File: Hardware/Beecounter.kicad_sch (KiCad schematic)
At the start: 142 parts, among them J1 Conn_01x03, J10 Conn_01x03, J11 Conn_01x03, J12 Conn_01x03, J13 Conn_01x03, J14 Conn_01x03, J15 Conn_02x20_Odd_Even, J2 Conn_01x03, J3 Conn_01x03, J4 Conn_01x03, J5 Conn_01x03, J6 Conn_01x03, J7 Conn_01x03, J8 Conn_01x03, J9 Conn_01x03, U1 LM393, U10 LM393, U11 H2010, U12 LM393, U13 H2010, U14 LM393, U15 H2010, U16 LM393, U17 H2010, U18 LM393, U19 H2010, U2 H2010, U20 LM393, U21 H2010, U22 LM393, U23 H2010, U24 LM393, U25 H2010, U26 LM393, U27 H2010, U28 LM393, U3 H2010, U4 LM393, U5 H2010, U6 LM393, U7 H2010, U8 LM393, U9 H2010

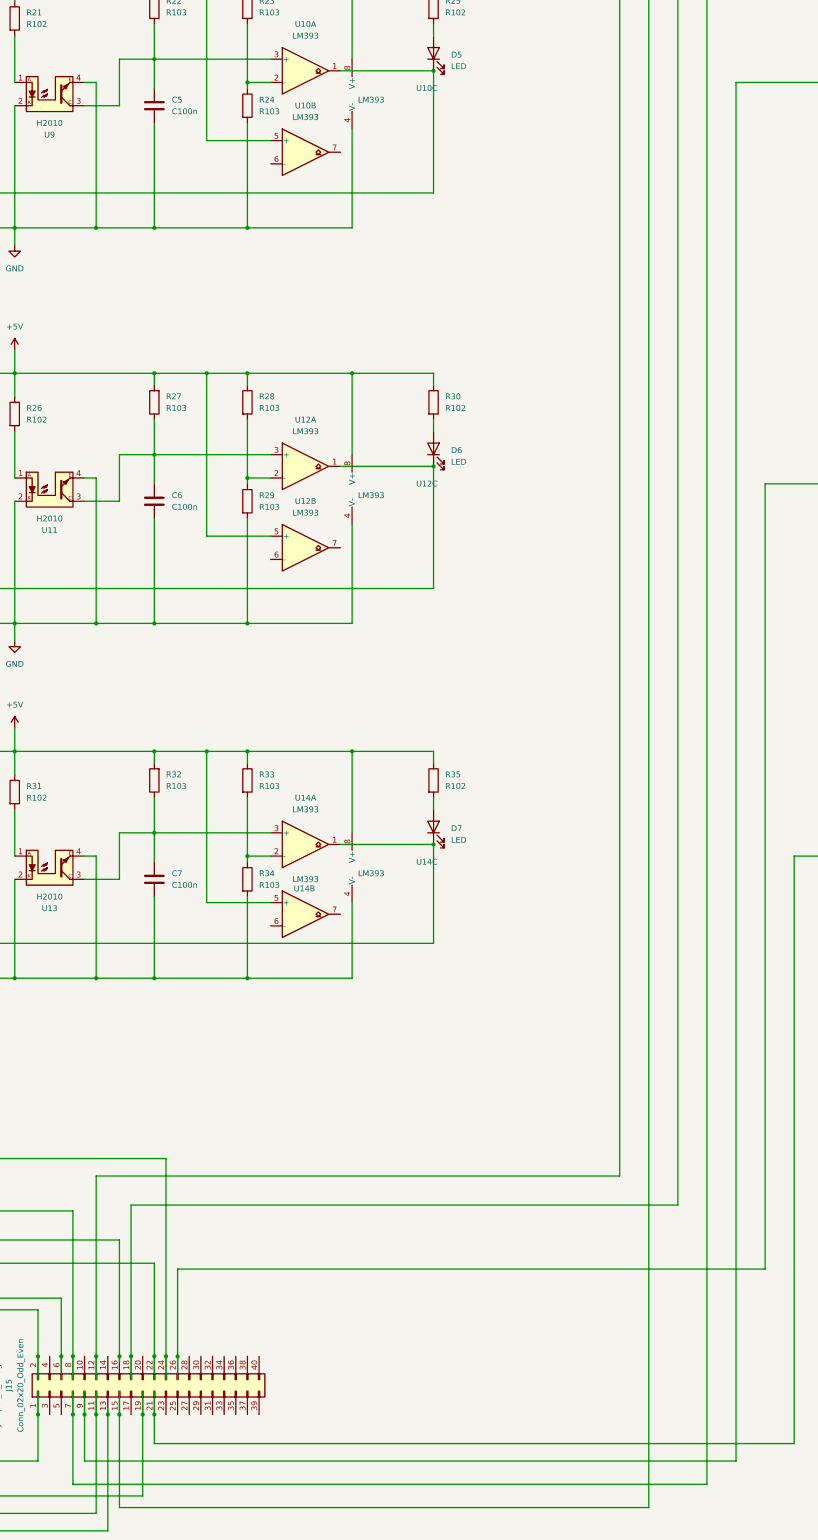
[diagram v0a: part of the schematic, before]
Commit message: Fix issue with entrance 5. Connected light barrier to pin 10 (GPIO16) instead of 9 (GND)
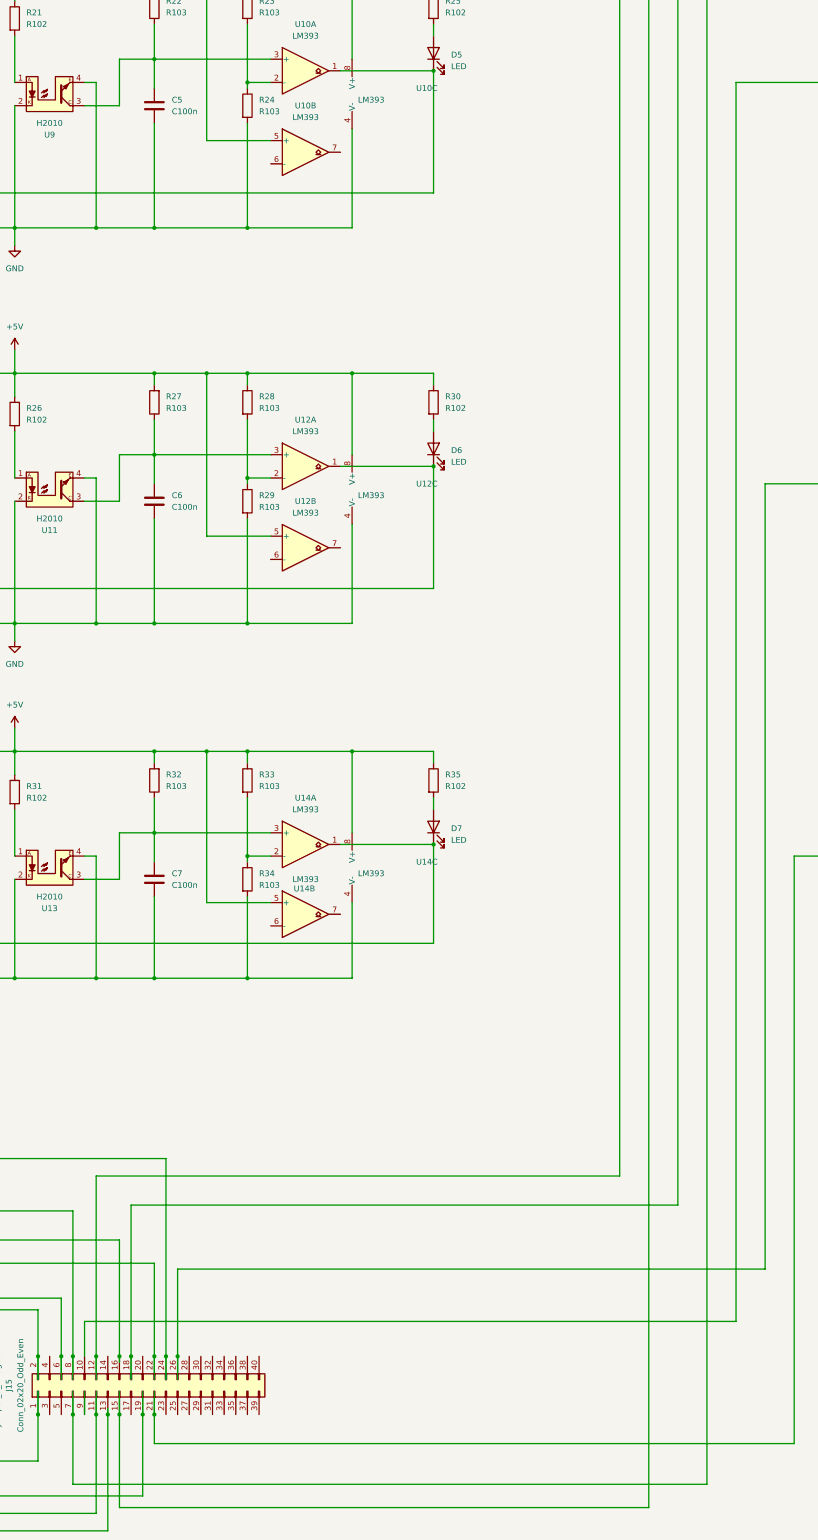
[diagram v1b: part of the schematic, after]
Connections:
- net at D12.1 (K), J12.2 (Pin_2), U24.1: now also J15.10 (Pin_10); no longer J15.9 (Pin_9)
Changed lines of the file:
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@@
 	)
 	(junction
-		(at 171.45 676.91)
-		(diameter 0)
-		(color 0 0 0 0)
-	)
-	(junction
 		(at 179.07 664.21)
 		(diameter 0)
@@
 	(wire
 		(pts
-			(xy 313.69 687.07) (xy 171.45 687.07)
+			(xy 313.69 656.59) (xy 171.45 656.59)
 		)
 		(stroke
@@
 	(wire
 		(pts
-			(xy 171.45 676.91) (xy 171.45 687.07)
-		)
-		(stroke
-			(width 0)
-			(type default)
-		)
-	)
-	(wire
-		(pts
 			(xy 80.01 474.98) (xy 133.35 474.98)
 		)
@@
 	(wire
 		(pts
-			(xy 313.69 386.08) (xy 313.69 687.07)
+			(xy 313.69 386.08) (xy 313.69 656.59)
 		)
 		(stroke
@@
 		)
 		(stroke
+			(width 0)
+			(type default)
+		)
+	)
+	(wire
+		(pts
+			(xy 171.45 656.59) (xy 171.45 664.21)
+		)
+		(stroke

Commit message: Set power supply for light barriers to 3.3V
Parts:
- removed JP1: Jumper_3_Bridged12, Jumper:SolderJumper-3_P1.3mm_Open_RoundedPad1.0x1.5mm, symbol Jumper:Jumper_3_Bridged12
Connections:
- net +5V is gone; now on net +3.3V: J1.1 (Pin_1), J10.1 (Pin_1), J11.1 (Pin_1), J12.1 (Pin_1), J13.1 (Pin_1), J14.1 (Pin_1), J2.1 (Pin_1), J3.1 (Pin_1), J4.1 (Pin_1), J5.1 (Pin_1), J6.1 (Pin_1), J7.1 (Pin_1), J8.1 (Pin_1), J9.1 (Pin_1), R1.1, R10.1, R11.1, R12.2, R13.1, R15.1, R16.1, R17.2, R18.1, R2.1, R20.1, R21.1, R22.2, R23.1, R25.1, R26.1, R27.2, R28.1, R30.1, R31.1, R32.2, R33.1, R35.1, R36.1, R37.2, R38.1, R4.2, R40.1, R41.1, R42.2, R43.1, R45.1, R46.1, R47.2, R48.1, R5.1, R50.1, R51.1, R52.2, R53.1, R55.1, R56.1, R57.2, R58.1, R6.1, R60.1, R61.1, R62.2, R63.1, R65.1, R66.1, R67.2, R68.1, R7.2, R70.1, R8.1, U1.5 (+), U1.8 (V+), U10.5 (+), U10.8 (V+), U12.5 (+), U12.8 (V+), U14.5 (+), U14.8 (V+), U16.5 (+), U16.8 (V+), U18.5 (+), U18.8 (V+), U20.5 (+), U20.8 (V+), U22.5 (+), U22.8 (V+), U24.5 (+), U24.8 (V+), U26.5 (+), U26.8 (V+), U28.5 (+), U28.8 (V+), U4.5 (+), U4.8 (V+), U6.5 (+), U6.8 (V+), U8.5 (+), U8.8 (V+)
- net +3.3V: now reaches J15.1 (Pin_1)
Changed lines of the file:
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@@
 	)
 	(junction
-		(at 161.29 664.21)
-		(diameter 0)
-		(color 0 0 0 0)
-	)
-	(junction
 		(at 198.12 36.83)
 		(diameter 0)
@@
 	)
 	(junction
-		(at 142.24 670.56)
-		(diameter 0)
-		(color 0 0 0 0)
-	)
-	(junction
 		(at 459.74 59.69)
 		(diameter 0)
@@
 	)
 	(junction
-		(at 146.05 676.91)
-		(diameter 0)
-		(color 0 0 0 0)
-	)
-	(junction
 		(at 436.88 250.19)
 		(diameter 0)
@@
 	)
 	(junction
-		(at 146.05 664.21)
-		(diameter 0)
-		(color 0 0 0 0)
-	)
-	(junction
 		(at 454.66 415.29)
 		(diameter 0)
@@
 	(wire
 		(pts
-			(xy 161.29 687.07) (xy 146.05 687.07)
-		)
-		(stroke
-			(width 0)
-			(type default)
-		)
-	)
-	(wire
-		(pts
 			(xy 156.21 477.52) (xy 156.21 504.19)
 		)
@@
 	(wire
 		(pts
-			(xy 146.05 664.21) (xy 146.05 665.48)
-		)
-		(stroke
-			(width 0)
-			(type default)
-		)
-	)
-	(wire
-		(pts
 			(xy 453.39 529.59) (xy 453.39 532.13)
 		)
@@
 	(wire
 		(pts
-			(xy 142.24 670.56) (xy 144.78 670.56)
-		)
-		(stroke
-			(width 0)
-			(type default)
-		)
-	)
-	(wire
-		(pts
 			(xy 184.15 694.69) (xy 184.15 676.91)
 		)
@@
 	(wire
 		(pts
-			(xy 146.05 675.64) (xy 146.05 676.91)
-		)
-		(stroke
-			(width 0)
-			(type default)
-		)
-	)
-	(wire
-		(pts
 			(xy 477.52 481.33) (xy 477.52 502.92)
 		)
@@
 	(wire
 		(pts
-			(xy 161.29 654.05) (xy 146.05 654.05)
-		)
-		(stroke
-			(width 0)
-			(type default)
-		)
-	)
-	(wire
-		(pts
 			(xy 478.79 278.13) (xy 496.57 278.13)
 		)
@@
 	(wire
 		(pts
-			(xy 146.05 687.07) (xy 146.05 676.91)
-		)
-		(stroke
-			(width 0)
-			(type default)
-		)
-	)
-	(wire
-		(pts
 			(xy 434.34 466.09) (xy 434.34 472.44)
 		)
@@
 	(wire
 		(pts
-			(xy 146.05 664.21) (xy 146.05 654.05)
-		)
-		(stroke
-			(width 0)
-			(type default)
-		)
-	)
-	(wire
-		(pts
 			(xy 133.35 472.44) (xy 140.97 472.44)
 		)
@@
 	(wire
 		(pts
-			(xy 118.11 670.56) (xy 142.24 670.56)
+			(xy 118.11 687.07) (xy 161.29 687.07)
 		)
 		(stroke
@@
 	(wire
 		(pts
-			(xy 161.29 664.21) (xy 161.29 654.05)
-		)
-		(stroke
-			(width 0)
-			(type default)
-		)
-	)
-	(wire
-		(pts
 			(xy 403.86 415.29) (xy 421.64 415.29)
 		)
@@
 	(wire
 		(pts
-			(xy 118.11 670.56) (xy 118.11 554.99)
+			(xy 118.11 687.07) (xy 118.11 554.99)
 		)
 		(stroke
@@
 			)
 		)
-		(property "Value" "+5V"
+		(property "Value" "+3.3V"
 			(at 156.21 353.06 0)
 			(effects
@@
 			)
 		)
-		(property "Value" "+5V"
+		(property "Value" "+3.3V"
 			(at 403.86 350.52 0)
 			(effects
@@
 			)
 		)
-		(property "Value" "+5V"
+		(property "Value" "+3.3V"
 			(at 407.67 102.87 0)
 			(effects
@@
 			)
 		)
-		(property "Value" "+5V"
+		(property "Value" "+3.3V"
 			(at 403.86 438.15 0)
 			(effects
@@
 			)
 		)
-		(property "Value" "+5V"
+		(property "Value" "+3.3V"
 			(at 156.21 270.51 0)
 			(effects
@@
 	)
 	(symbol
-		(lib_id "Jumper:Jumper_3_Bridged12")
-		(at 146.05 670.56 270)
-		(unit 1)
-		(exclude_from_sim yes)
-		(in_bom no)
-		(on_board yes)
-		(dnp no)
-		(fields_autoplaced yes)
-		(property "Reference" "JP1"
-			(at 149.86 670.56 0)
-			(effects
-				(font
-					(size 1.27 1.27)
-				)
-			)
-		)
-		(property "Value" "Jumper_3_Bridged12"
-			(at 152.4 670.56 0)
-			(effects
-				(font
-					(size 1.27 1.27)
-				)
-			)
-		)
-		(property "Footprint" "Jumper:SolderJumper-3_P1.3mm_Open_RoundedPad1.0x1.5mm"
-			(at 146.05 670.56 0)
-			(effects
-				(font
-					(size 1.27 1.27)
-				)
-				(hide yes)
-			)
-		)
-		(property "Datasheet" "~"
-			(at 146.05 670.56 0)
-			(effects
-				(font
-					(size 1.27 1.27)
-				)
-				(hide yes)
-			)
-		)
-		(property "Description" "Jumper, 3-pole, pins 1+2 closed/bridged"
-			(at 146.05 670.56 0)
-			(effects
-				(font
-					(size 1.27 1.27)
-				)
-				(hide yes)
-			)
-		)
-		(pin "1"
-		)
-		(pin "3"
-		)
-		(pin "2"
-		)
-		(instances
-			(project "Beecounter"
-				(path "/bf1fad0e-6a86-49c9-965e-c45578b7af4d"
-					(reference "JP1")
-					(unit 1)
-				)
-			)
-		)
-	)
-	(symbol
 		(lib_id "Sensor_Proximity:ITR9608-F")
 		(at 163.83 223.52 0)
@@
 			)
 		)
-		(property "Value" "+5V"
+		(property "Value" "+3.3V"
 			(at 156.21 187.96 0)
 			(effects
@@
 			)
 		)
-		(property "Value" "+5V"
+		(property "Value" "+3.3V"
 			(at 156.21 439.42 0)
 			(effects
@@
 			)
 		)
-		(property "Value" "+5V"
+		(property "Value" "+3.3V"
 			(at 402.59 519.43 0)
 			(effects
@@
 			)
 		)
-		(property "Value" "+5V"
+		(property "Value" "+3.3V"
 			(at 406.4 185.42 0)
 			(effects
@@
 			)
 		)
-		(property "Value" "+5V"
+		(property "Value" "+3.3V"
 			(at 156.21 26.67 0)
 			(effects
@@
 			)
 		)
-		(property "Value" "+5V"
+		(property "Value" "+3.3V"
 			(at 405.13 267.97 0)
 			(effects
@@
 			)
 		)
-		(property "Value" "+5V"
+		(property "Value" "+3.3V"
 			(at 156.21 521.97 0)
 			(effects
@@
 			)
 		)
-		(property "Value" "+5V"
+		(property "Value" "+3.3V"
 			(at 408.94 26.67 0)
 			(effects
@@
 			)
 		)
-		(property "Value" "+5V"
+		(property "Value" "+3.3V"
 			(at 156.21 105.41 0)
 			(effects

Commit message: Exchanged pin 16 and 18
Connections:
- net at D10.1 (K), J10.2 (Pin_2), U20.1: now also J15.16 (Pin_16); no longer J15.18 (Pin_18)
- net at D3.1 (K), J3.2 (Pin_2), U6.1: now also J15.18 (Pin_18); no longer J15.16 (Pin_16)
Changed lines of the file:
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@@
 	)
 	(junction
+		(at 179.07 664.21)
+		(diameter 0)
+		(color 0 0 0 0)
+	)
+	(junction
 		(at 434.34 378.46)
 		(diameter 0)
@@
 	)
 	(junction
+		(at 181.61 664.21)
+		(diameter 0)
+		(color 0 0 0 0)
+	)
+	(junction
 		(at 173.99 676.91)
 		(diameter 0)
@@
 	)
 	(junction
-		(at 181.61 664.21)
-		(diameter 0)
-		(color 0 0 0 0)
-	)
-	(junction
 		(at 186.69 504.19)
 		(diameter 0)
@@
 	)
 	(junction
-		(at 179.07 664.21)
-		(diameter 0)
-		(color 0 0 0 0)
-	)
-	(junction
 		(at 207.01 554.99)
 		(diameter 0)
@@
 	(wire
 		(pts
-			(xy 60.96 223.52) (xy 60.96 638.81)
+			(xy 63.5 223.52) (xy 63.5 638.81)
 		)
 		(stroke
@@
 	(wire
 		(pts
-			(xy 300.99 631.19) (xy 181.61 631.19)
-		)
-		(stroke
-			(width 0)
-			(type default)
-		)
-	)
-	(wire
-		(pts
 			(xy 140.97 417.83) (xy 156.21 417.83)
 		)
@@
 	(wire
 		(pts
+			(xy 179.07 631.19) (xy 179.07 664.21)
+		)
+		(stroke
+			(width 0)
+			(type default)
+		)
+	)
+	(wire
+		(pts
 			(xy 156.21 203.2) (xy 156.21 198.12)
 		)
@@
 	(wire
 		(pts
-			(xy 179.07 638.81) (xy 179.07 664.21)
-		)
-		(stroke
-			(width 0)
-			(type default)
-		)
-	)
-	(wire
-		(pts
 			(xy 455.93 278.13) (xy 455.93 280.67)
 		)
@@
 	(wire
 		(pts
+			(xy 63.5 638.81) (xy 181.61 638.81)
+		)
+		(stroke
+			(width 0)
+			(type default)
+		)
+	)
+	(wire
+		(pts
 			(xy 140.97 477.52) (xy 140.97 504.19)
 		)
@@
 	(wire
 		(pts
-			(xy 181.61 631.19) (xy 181.61 664.21)
-		)
-		(stroke
-			(width 0)
-			(type default)
-		)
-	)
-	(wire
-		(pts
 			(xy 434.34 360.68) (xy 445.77 360.68)
 		)
@@
 	(wire
 		(pts
-			(xy 60.96 223.52) (xy 133.35 223.52)
+			(xy 63.5 223.52) (xy 133.35 223.52)
 		)
 		(stroke
@@
 	(wire
 		(pts
-			(xy 60.96 638.81) (xy 179.07 638.81)
-		)
-		(stroke
-			(width 0)
-			(type default)
-		)
-	)
-	(wire
-		(pts
 			(xy 439.42 91.44) (xy 459.74 91.44)
 		)
@@
 	(wire
 		(pts
+			(xy 179.07 631.19) (xy 300.99 631.19)
+		)
+		(stroke
+			(width 0)
+			(type default)
+		)
+	)
+	(wire
+		(pts
 			(xy 383.54 220.98) (xy 396.24 220.98)
 		)
@@
 		)
 		(stroke
+			(width 0)
+			(type default)
+		)
+	)
+	(wire
+		(pts
+			(xy 181.61 664.21) (xy 181.61 638.81)
+		)
+		(stroke

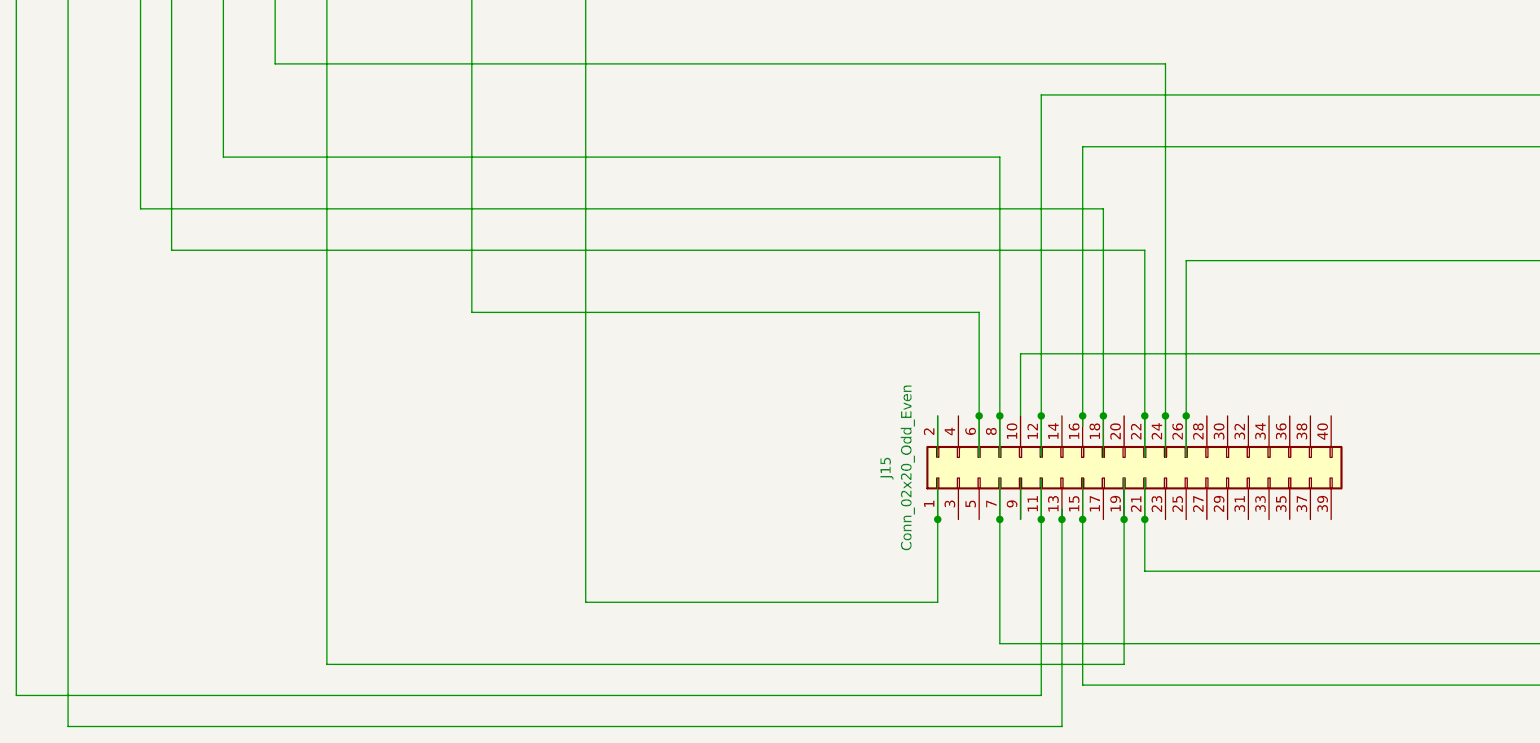
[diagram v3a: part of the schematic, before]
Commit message: Connected GND pins
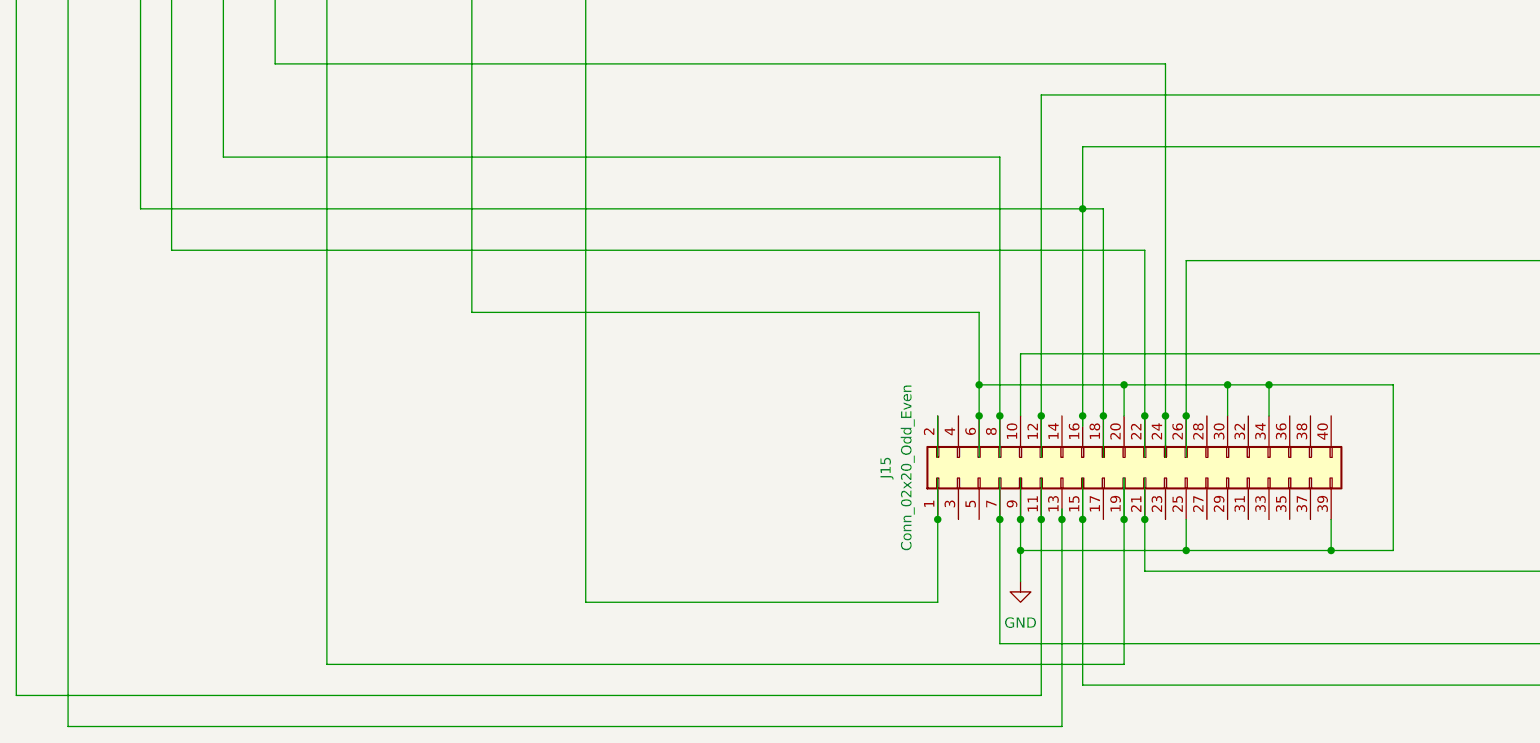
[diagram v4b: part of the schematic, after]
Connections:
- net GND: now also J15.20 (Pin_20), J15.25 (Pin_25), J15.30 (Pin_30), J15.34 (Pin_34), J15.39 (Pin_39), J15.9 (Pin_9)
- net at D10.1 (K), J10.2 (Pin_2), J15.16 (Pin_16)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: now also D3.1 (K), J15.18 (Pin_18), J3.2 (Pin_2), U6.1
